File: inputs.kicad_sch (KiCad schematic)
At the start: 110 parts, among them U6 74HC14, U7 74HC14, U8 74HC14

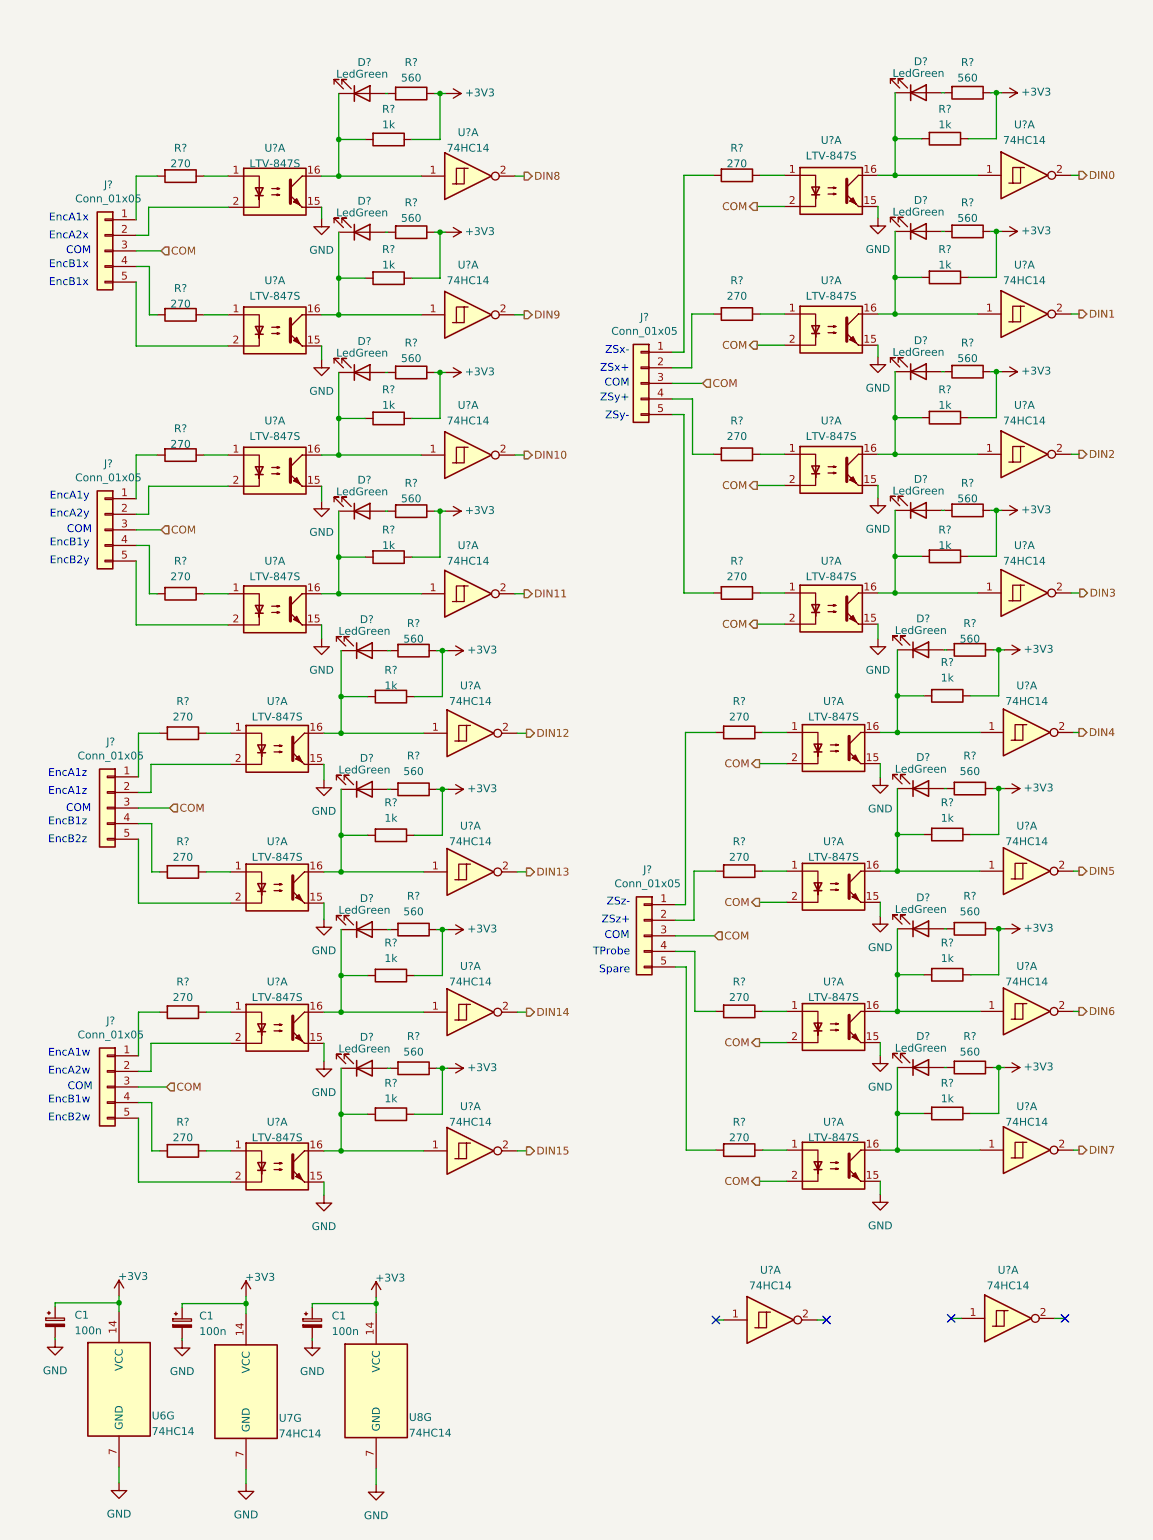
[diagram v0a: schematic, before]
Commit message: Avances en corrección de errores en conexiones eléctricas (ERC).
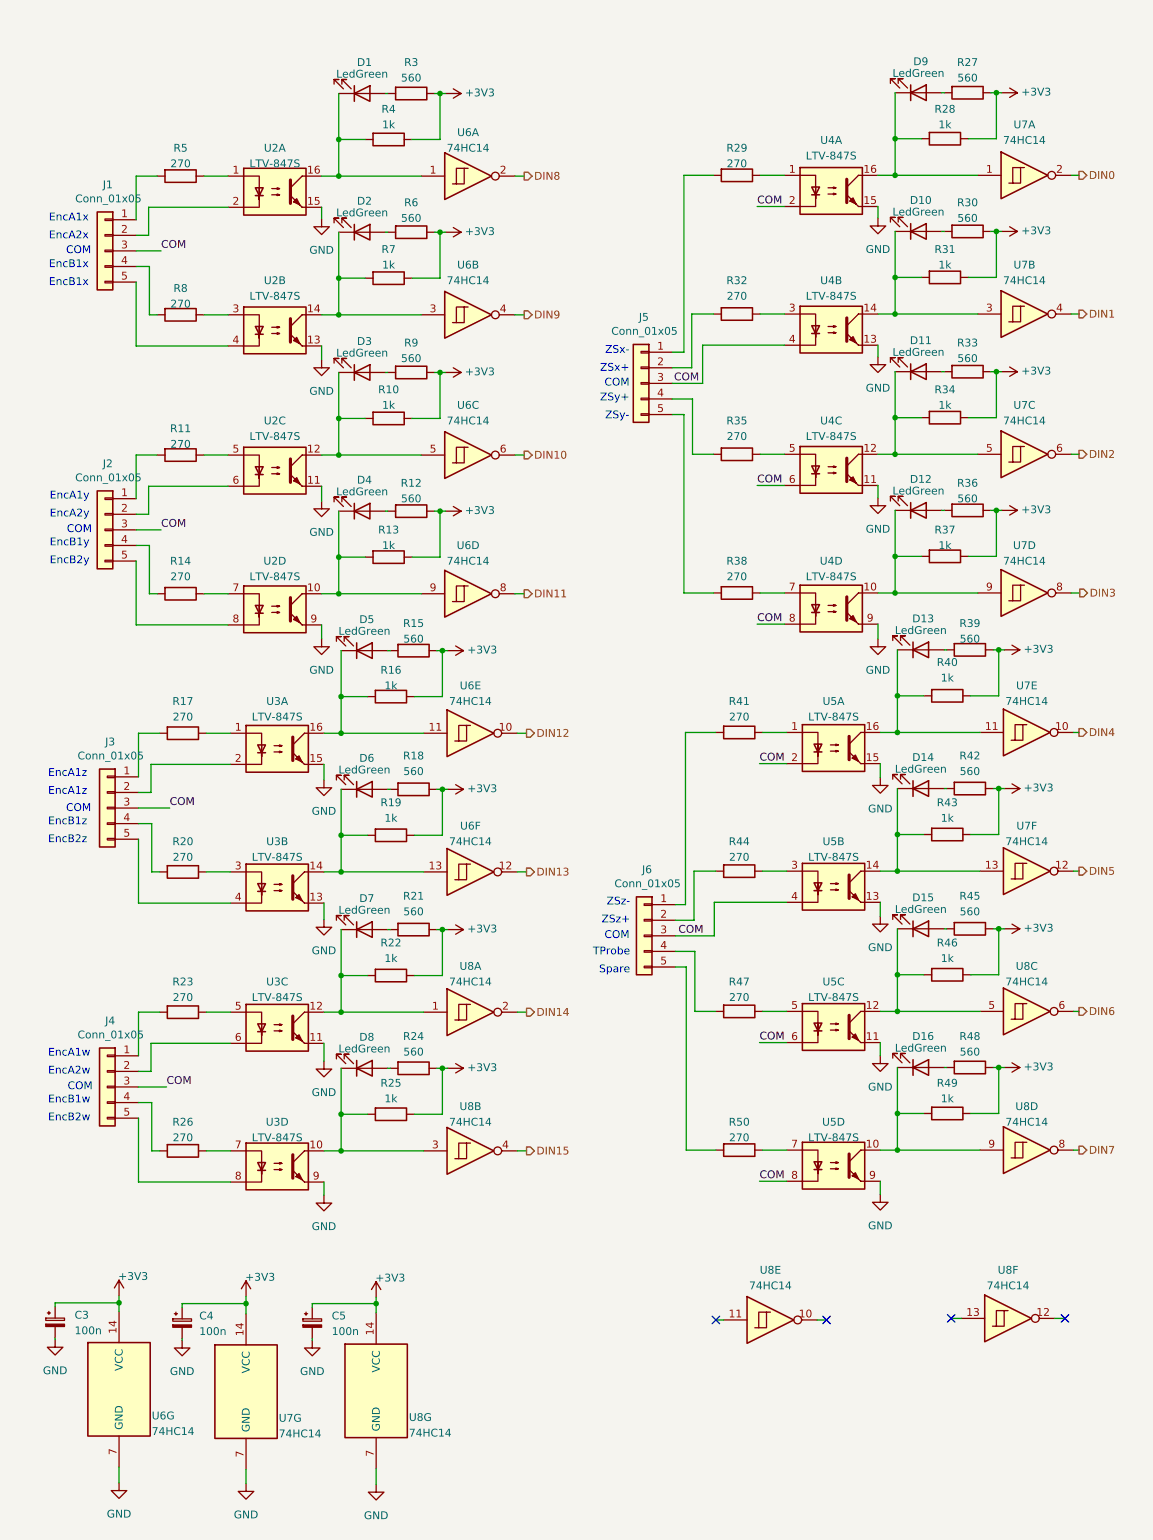
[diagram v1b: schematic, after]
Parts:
- gave numbers to parts that had none: 77
- renumbered C1 to C3, C1 to C4, C1 to C5
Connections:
- net COM: now also U4.4, U4.6, U4.8, U5.4, U5.6, U5.8; no longer U4.2, U4.2, U4.2, U5.2, U5.2, U5.2
- net DIN1: now also U7.4; no longer U7.2
- net DIN10: now also U6.6; no longer U6.2
- net DIN11: now also U6.8; no longer U6.2
- net DIN12: now also U6.10; no longer U6.2
- net DIN13: now also U6.12; no longer U6.2
- net DIN15: now also U8.4; no longer U8.2
- net DIN2: now also U7.6; no longer U7.2
- net DIN3: now also U7.8; no longer U7.2
- net DIN4: now also U7.10; no longer U7.2
- net DIN5: now also U7.12; no longer U7.2
- net DIN6: now also U8.6; no longer U8.2
- net DIN7: now also U8.8; no longer U8.2
- net DIN9: now also U6.4; no longer U6.2
- net GND: now also U2.11, U2.13, U2.9, U3.11, U3.13, U3.9, U4.11, U4.13, U4.9, U5.11, U5.13, U5.9; no longer U2.15, U2.15, U2.15, U3.15, U3.15, U3.15, U4.15, U4.15, U4.15, U5.15, U5.15, U5.15
- net at D5.1 (K), R16.2, U3.16: now also U6.11; no longer U6.1
- net at R44.1: now also U5.3; no longer U5.1
- net at D14.1 (K), R43.2: now also U5.14, U7.13; no longer U5.16, U7.1
- net at D8.1 (K), R25.2: now also U3.10, U8.3; no longer U3.16, U8.1
- net at R23.1: now also U3.5; no longer U3.1
- net at D7.1 (K), R22.2, U8.1: now also U3.12; no longer U3.16
- net at J4.2 (Pin_2): now also U3.6; no longer U3.2
- net at R14.1: now also U2.7; no longer U2.1
- net at D2.1 (K), R7.2: now also U2.14, U6.3; no longer U2.16, U6.1
- net at D16.1 (K), R49.2: now also U5.10, U8.9; no longer U5.16, U8.1
- net at R11.1: now also U2.5; no longer U2.1
- net at R26.1: now also U3.7; no longer U3.1
- net at J4.5 (Pin_5): now also U3.8; no longer U3.2
- net at D4.1 (K), R13.2: now also U2.10, U6.9; no longer U2.16, U6.1
- net at D12.1 (K), R37.2: now also U4.10, U7.9; no longer U4.16, U7.1
- net at J2.5 (Pin_5): now also U2.8; no longer U2.2
- net at R32.1: now also U4.3; no longer U4.1
- net at D6.1 (K), R19.2: now also U3.14, U6.13; no longer U3.16, U6.1
- net at D3.1 (K), R10.2: now also U2.12, U6.5; no longer U2.16, U6.1
- net at D11.1 (K), R34.2: now also U4.12, U7.5; no longer U4.16, U7.1
- net at R20.1: now also U3.3; no longer U3.1
- net at J3.5 (Pin_5): now also U3.4; no longer U3.2
- net at D13.1 (K), R40.2, U5.16: now also U7.11; no longer U7.1
- net at R35.1: now also U4.5; no longer U4.1
- net at J2.2 (Pin_2): now also U2.6; no longer U2.2
- net at R8.1: now also U2.3; no longer U2.1
- net at R47.1: now also U5.5; no longer U5.1
- net at R50.1: now also U5.7; no longer U5.1
- net at J1.5 (Pin_5): now also U2.4; no longer U2.2
- net at R38.1: now also U4.7; no longer U4.1
- net at D10.1 (K), R31.2: now also U4.14, U7.3; no longer U4.16, U7.1
- net at D15.1 (K), R46.2: now also U5.12, U8.5; no longer U5.16, U8.1

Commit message: Se corrigieron errores de conexión. Falta asignar footprints aún
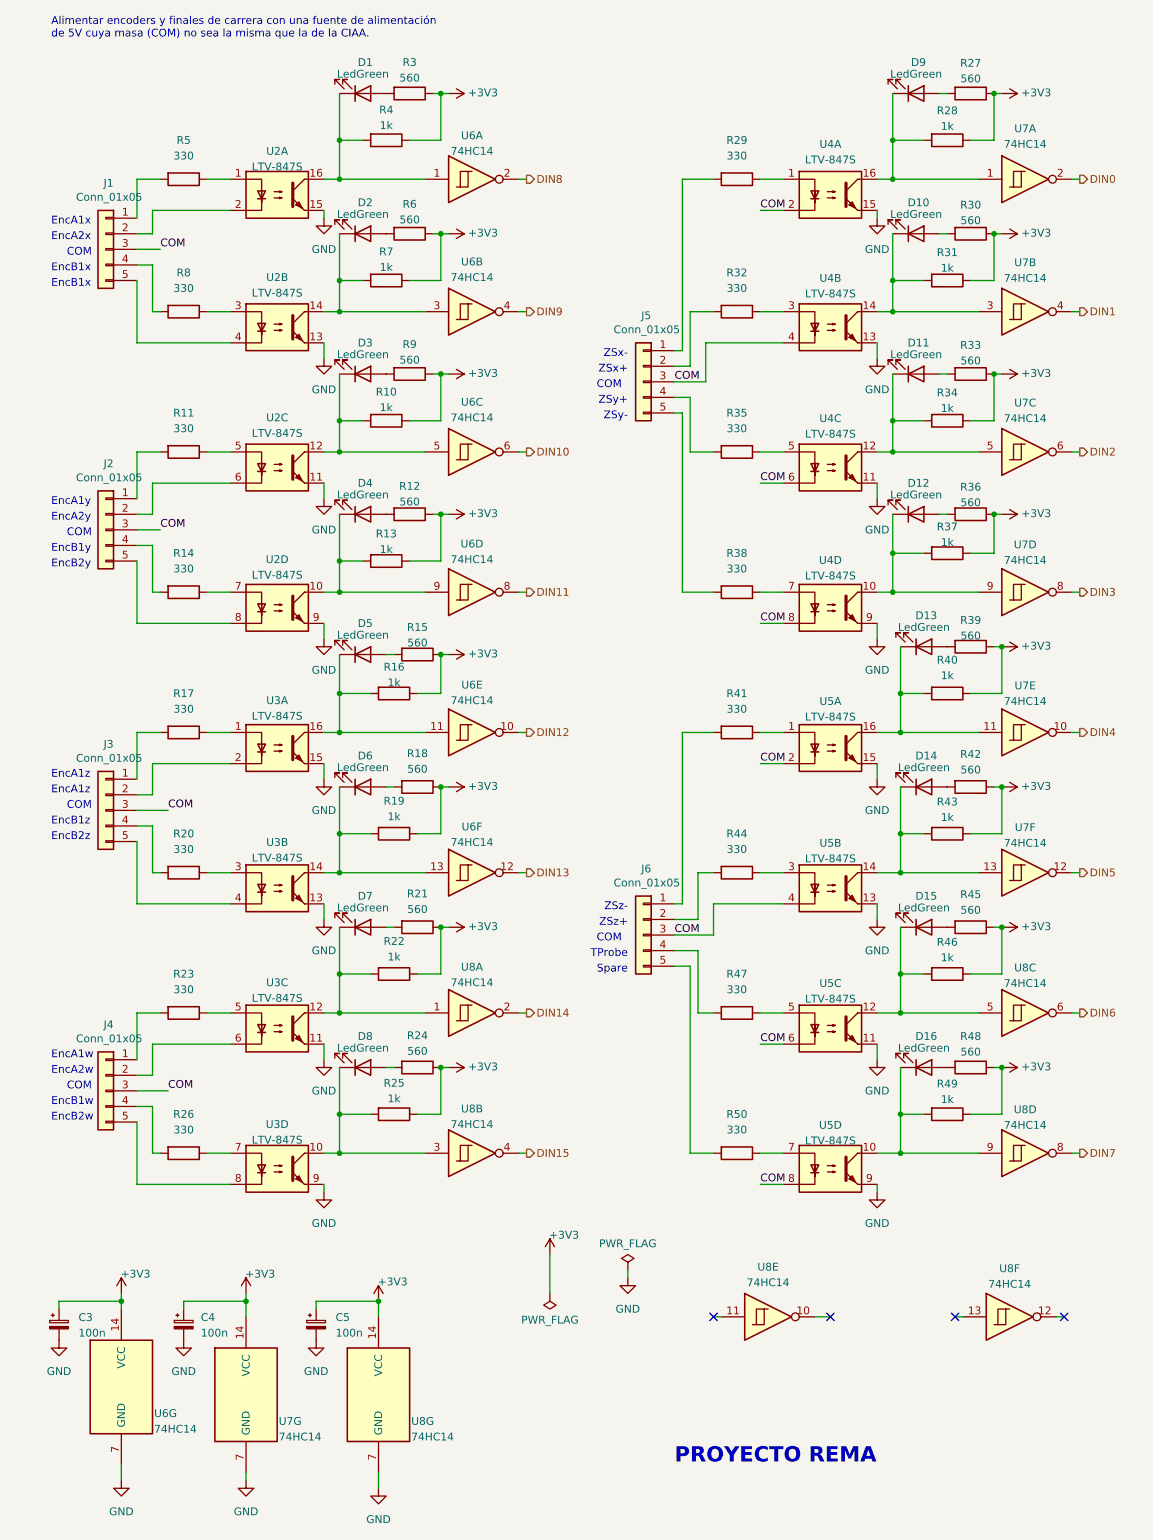
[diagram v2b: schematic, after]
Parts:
- D1, D10, D11, D12, D13, D14, D15, D16, D2, D3, D4, D5, D6, D7, D8, D9: footprint (none) -> LED_SMD:LED_1206_3216Metric
- R11, R14, R17, R20, R23, R26, R29, R32, R35, R38, R41, R44, R47, R5, R50, R8: value 270 -> 330
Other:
- note added: "Alimentar encoders y finales de carrera con una fuente de alimentación de 5V cuya masa (COM) no sea la misma que la de la CIAA."
- note added: "PROYECTO REMA"
- title: (none) -> Entradas
- moved on the sheet: C3, C5, D10, D11, D12, D13, D14, D15, D16, D4, D5, J4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

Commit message: Esquemático listo, sin errores de conexión y con todos los footprints especificados
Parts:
- C3, C4, C5: footprint (none) -> Capacitor_SMD:C_1206_3216Metric
- J1, J2, J3, J4, J5, J6: footprint (none) -> Connector_PinHeader_2.54mm:PinHeader_1x05_P2.54mm_Vertical
- R10, R11, R12, R13, R14, R15, R16, R17, R18, R19, R20, R21, R22, R23, R24, R25, R26, R27, R28, R29, R3, R30, R31, R32, R33, R34, R35, R36, R37, R38, R39, R4, R40, R41, R42, R43, R44, R45, R46, R47, R48, R49, R5, R50, R6, R7, R8, R9: footprint (none) -> Resistor_SMD:R_1206_3216Metric
- U6, U7, U8: footprint (none) -> Package_SO:SOIC-14-16_3.9x9.9mm_P1.27mm

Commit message: Comienza el diseño del pcb
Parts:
- added TP0, TP3: TestPoint, TestPoint:TestPoint_Pad_D2.0mm, symbol Connector:TestPoint
- U6, U7, U8: footprint Package_SO:SOIC-14-16_3.9x9.9mm_P1.27mm -> Package_SO:SOIC-14_3.9x8.7mm_P1.27mm
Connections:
- net +3V3: now also TP3.1
- net GND: now also TP0.1
